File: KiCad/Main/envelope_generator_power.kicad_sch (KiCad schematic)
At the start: 13 parts, among them U5 TL074, U6 TL074, U7 TL074

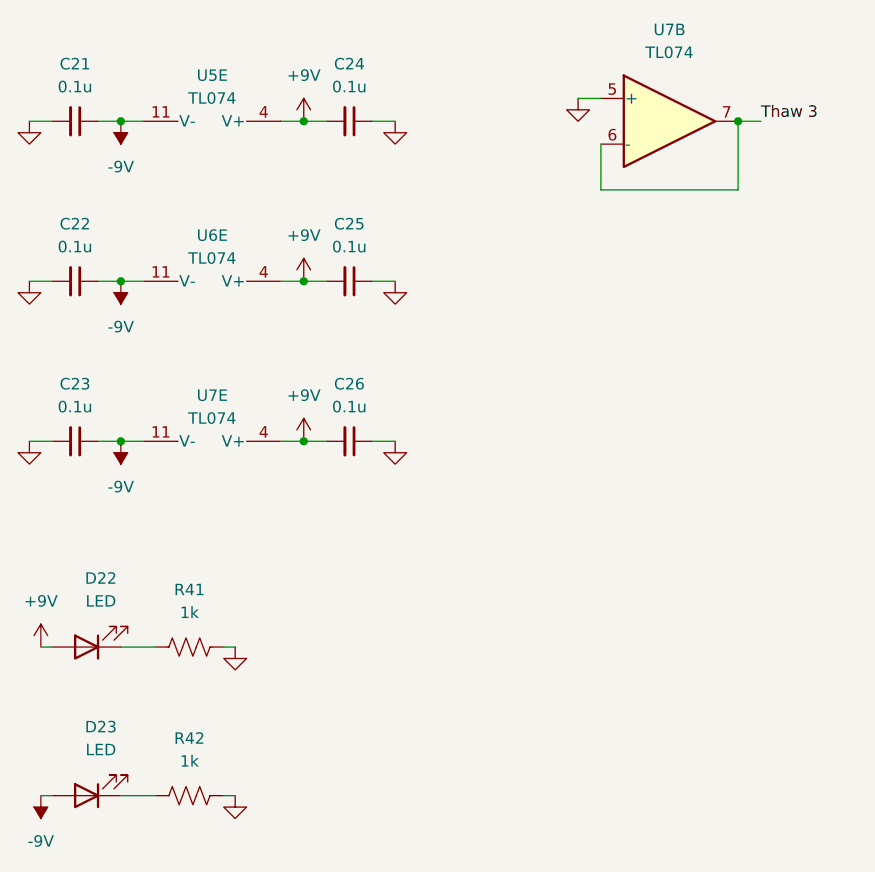
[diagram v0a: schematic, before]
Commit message: merged project into one combined board (excluding the buttons)
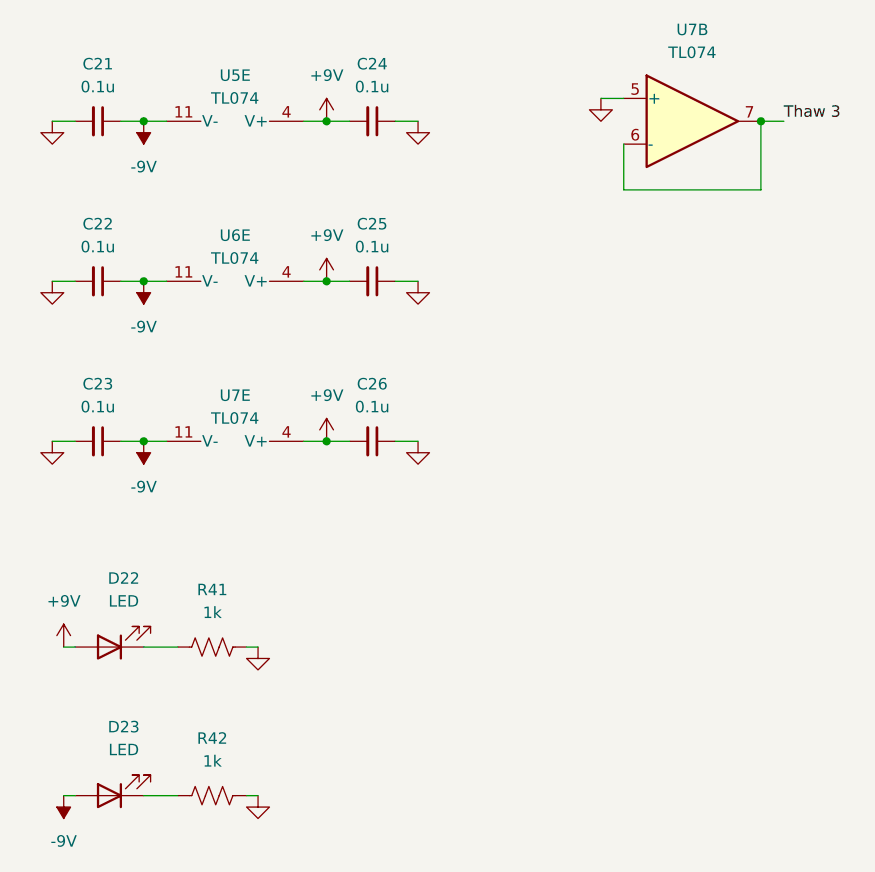
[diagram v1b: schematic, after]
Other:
- moved on the sheet: C25, D22, D23, R41, R42
